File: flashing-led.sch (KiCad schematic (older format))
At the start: 6 parts, among them U1 NE555

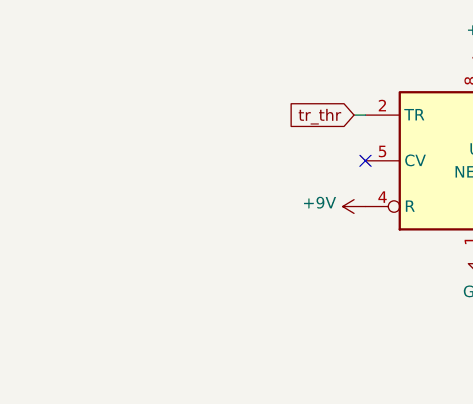
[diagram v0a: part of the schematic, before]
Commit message: Assigned PCB footprints to schematic symbols
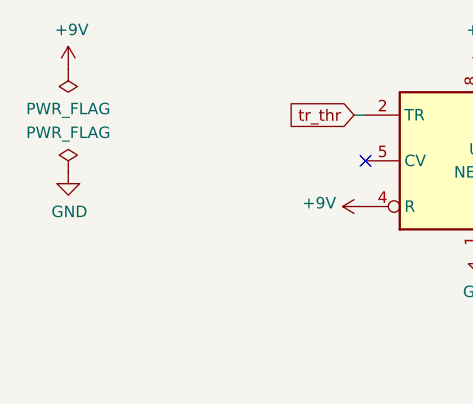
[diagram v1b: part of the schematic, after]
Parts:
- C1: footprint (none) -> Capacitor_SMD:CP_Elec_3x5.3
- D1: footprint (none) -> LED_SMD:LED-APA102-2020
- R1, R2, R3: footprint (none) -> Resistor_SMD:R_0201_0603Metric
- U1: footprint (none) -> Package_DIP:Fairchild_LSOP-8
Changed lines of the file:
@@
 F 0 "R2" H 4570 2396 50  0000 L CNN
 F 1 "470k" H 4570 2305 50  0000 L CNN
-F 2 "" V 4430 2350 50  0001 C CNN
+F 2 "Resistor_SMD:R_0201_0603Metric" V 4430 2350 50  0001 C CNN
 F 3 "~" H 4500 2350 50  0001 C CNN
 	1    4500 2350
@@
 F 0 "R1" H 4570 1796 50  0000 L CNN
 F 1 "1k" H 4570 1705 50  0000 L CNN
-F 2 "" V 4430 1750 50  0001 C CNN
+F 2 "Resistor_SMD:R_0201_0603Metric" V 4430 1750 50  0001 C CNN
 F 3 "~" H 4500 1750 50  0001 C CNN
 	1    4500 1750
@@
 F 0 "R3" H 4170 1896 50  0000 L CNN
 F 1 "1k" H 4170 1805 50  0000 L CNN
-F 2 "" V 4030 1850 50  0001 C CNN
+F 2 "Resistor_SMD:R_0201_0603Metric" V 4030 1850 50  0001 C CNN
 F 3 "~" H 4100 1850 50  0001 C CNN
 	1    4100 1850
@@
 F 0 "D1" V 4047 2228 50  0000 L CNN
 F 1 "LED" V 4138 2228 50  0000 L CNN
-F 2 "" H 4100 2150 50  0001 C CNN
+F 2 "LED_SMD:LED-APA102-2020" H 4100 2150 50  0001 C CNN
 F 3 "~" H 4100 2150 50  0001 C CNN
 	1    4100 2150
@@
 F 0 "C1" H 4618 2896 50  0000 L CNN
 F 1 "1uF" H 4618 2805 50  0000 L CNN
-F 2 "" H 4538 2700 50  0001 C CNN
+F 2 "Capacitor_SMD:CP_Elec_3x5.3" H 4538 2700 50  0001 C CNN
 F 3 "~" H 4500 2850 50  0001 C CNN
 	1    4500 2850
@@
 $EndComp
 $Comp
-L power:+9V #PWR0107
-U 1 1 5E2679C2
-P 3000 1500
-F 0 "#PWR0107" H 3000 1350 50  0001 C CNN
-F 1 "+9V" H 3015 1673 50  0000 C CNN
-F 2 "" H 3000 1500 50  0001 C CNN
-F 3 "" H 3000 1500 50  0001 C CNN
-	1    3000 1500
-	1    0    0    -1
-$EndComp
-$Comp
 L Timer:NE555 U1
 U 1 1 5E1FE6EE
@@
 F 0 "U1" H 3000 1950 50  0000 C CNN
 F 1 "NE555" H 3000 1850 50  0000 C CNN
-F 2 "" H 3000 1900 50  0001 C CNN
+F 2 "Package_DIP:Fairchild_LSOP-8" H 3000 1900 50  0001 C CNN
 F 3 "http://www.ti.com/lit/ds/symlink/ne555.pdf" H 3000 1900 50  0001 C CNN
 	1    3000 1900
 	1    0    0    -1
 $EndComp
+$Comp
+L power:PWR_FLAG #FLG0101
+U 1 1 5E24185A
+P 1200 1500
+F 0 "#FLG0101" H 1200 1575 50  0001 C CNN
+F 1 "PWR_FLAG" H 1200 1673 50  0000 C CNN
+F 2 "" H 1200 1500 50  0001 C CNN
+F 3 "~" H 1200 1500 50  0001 C CNN
+	1    1200 1500
+	-1   0    0    1
+$EndComp
+$Comp
+L power:+9V #PWR0107
+U 1 1 5E2679C2
+P 1200 1500
+F 0 "#PWR0107" H 1200 1350 50  0001 C CNN
+F 1 "+9V" H 1215 1673 50  0000 C CNN
+F 2 "" H 1200 1500 50  0001 C CNN
+F 3 "" H 1200 1500 50  0001 C CNN
+	1    1200 1500
+	1    0    0    -1
+$EndComp
+$Comp
+L power:+9V #PWR0101
+U 1 1 5E244E69
+P 3000 1500
+F 0 "#PWR0101" H 3000 1350 50  0001 C CNN
+F 1 "+9V" H 3015 1673 50  0000 C CNN
+F 2 "" H 3000 1500 50  0001 C CNN
+F 3 "" H 3000 1500 50  0001 C CNN
+	1    3000 1500
+	1    0    0    -1
+$EndComp
+$Comp
+L power:GND #PWR0103
+U 1 1 5E245BD7
+P 1200 1950
+F 0 "#PWR0103" H 1200 1700 50  0001 C CNN
+F 1 "GND" H 1205 1777 50  0000 C CNN
+F 2 "" H 1200 1950 50  0001 C CNN
+F 3 "" H 1200 1950 50  0001 C CNN
+	1    1200 1950
+	1    0    0    -1
+$EndComp
+$Comp
+L power:PWR_FLAG #FLG0102
+U 1 1 5E245E00
+P 1200 1950
+F 0 "#FLG0102" H 1200 2025 50  0001 C CNN
+F 1 "PWR_FLAG" H 1200 2123 50  0000 C CNN
+F 2 "" H 1200 1950 50  0001 C CNN
+F 3 "~" H 1200 1950 50  0001 C CNN
+	1    1200 1950
+	1    0    0    -1
+$EndComp

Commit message: updated schematic and pcb
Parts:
- removed U1: NE555, Package_DIP:Fairchild_LSOP-8, symbol Timer:NE555
- added J1: USB_B_Micro, Connector_USB:USB_Micro-B_Molex_47346-0001, symbol Connector:USB_B_Micro
- added U1: NE555D, Package_SO:SOIC-8_3.9x4.9mm_P1.27mm, symbol Timer:NE555D
- D1: footprint LED_SMD:LED-APA102-2020 -> LED_SMD:LED_0805_2012Metric
- R1: value 1k -> 100k; footprint Resistor_SMD:R_0201_0603Metric -> Resistor_SMD:R_0805_2012Metric
- R2: footprint Resistor_SMD:R_0201_0603Metric -> Resistor_SMD:R_0805_2012Metric
- R3: value 1k -> 270k; footprint Resistor_SMD:R_0201_0603Metric -> Resistor_SMD:R_0805_2012Metric
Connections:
- net GND: now also J1.5 (GND), J1.6 (Shield), U1.1 (GND)
- net dis: now also U1.7 (DIS)
- net tr_thr: now also U1.2 (TR), U1.6 (THR)
- net at R3.2: now also U1.3 (Q)
- net +9V renamed +5V
- net +5V: now also J1.1 (VBUS), U1.4 (R), U1.8 (VCC)
- no-connect marks 1 -> 4
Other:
- moved on the sheet: C1, D1, R1, R2, R3
